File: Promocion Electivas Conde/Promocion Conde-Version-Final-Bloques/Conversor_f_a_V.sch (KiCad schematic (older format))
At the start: 14 parts, among them J2 Bornera Señal de Entrada, Q1 BC848, U2 4040, U3 4070, U4 TL082

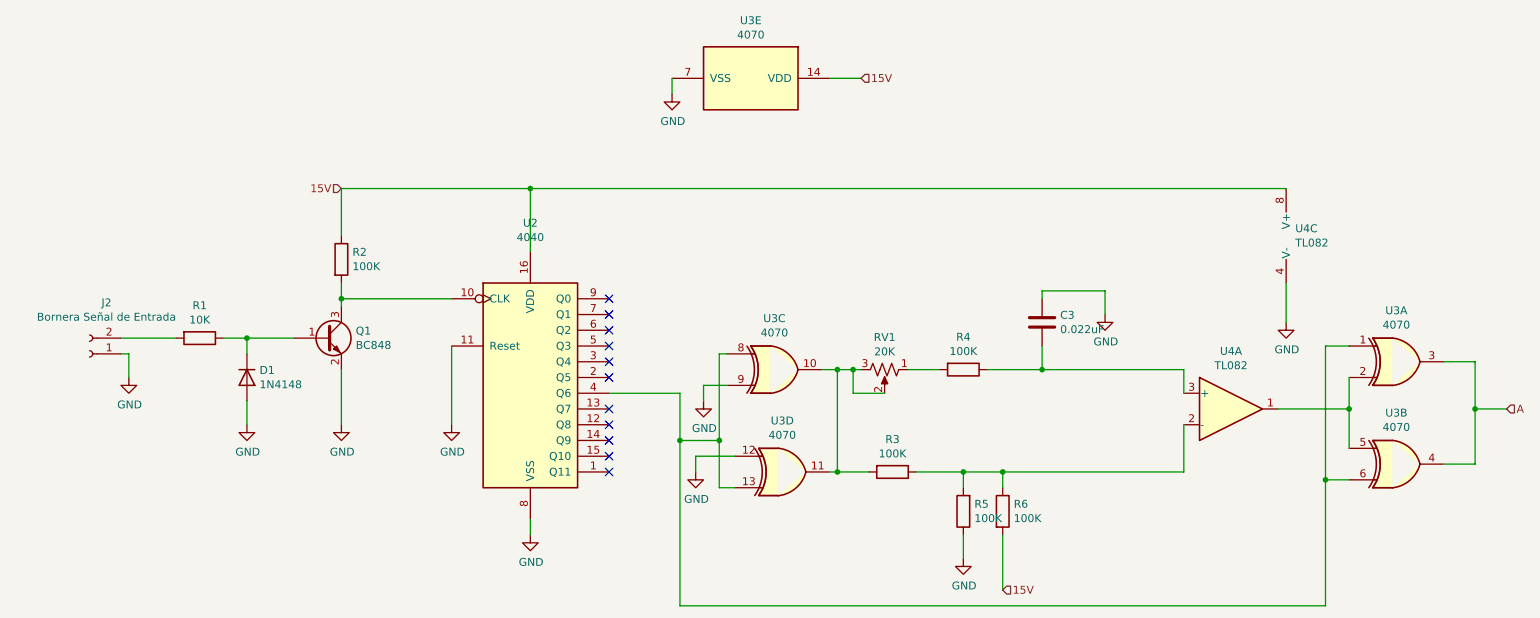
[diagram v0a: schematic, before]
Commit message: Agregue circuito 4-20 mA a la version en bloques
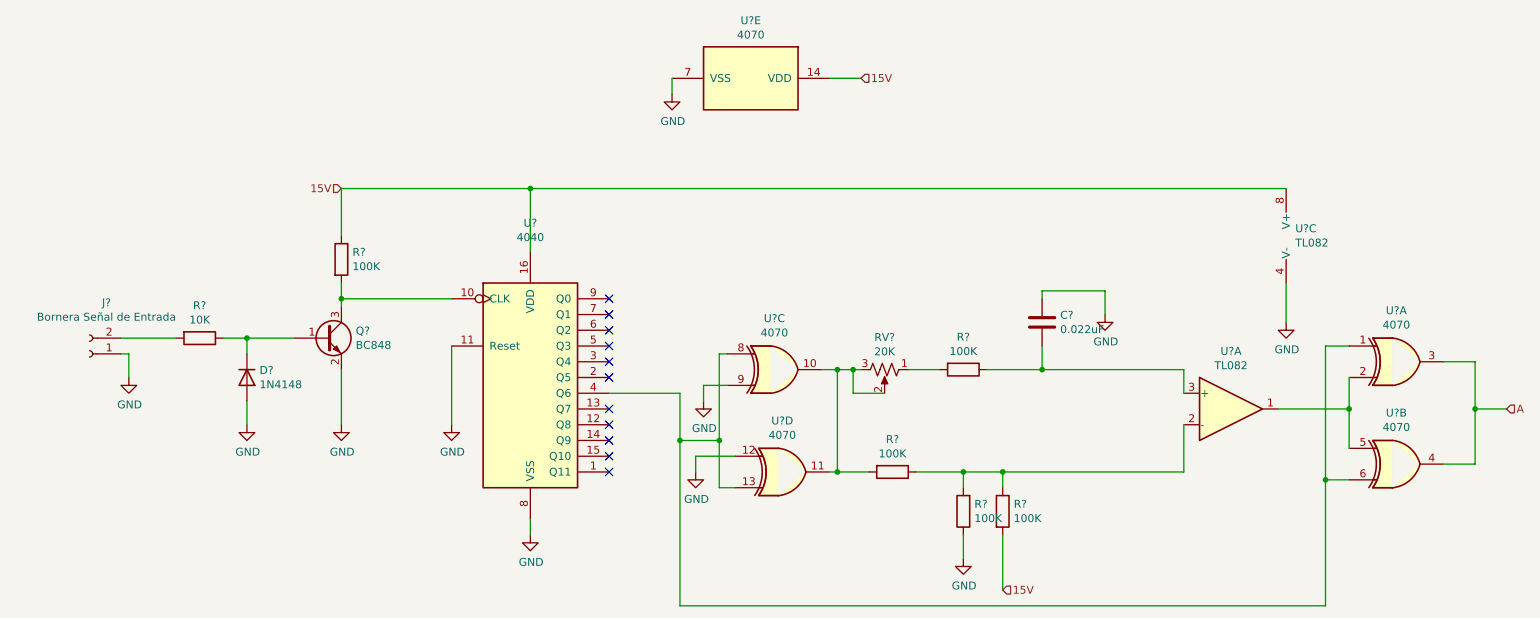
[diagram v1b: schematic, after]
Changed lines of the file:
@@
 $Descr A4 11693 8268
 encoding utf-8
-Sheet 2 4
+Sheet 5 5
 Title ""
 Date ""
@@
 AR Path="/61312797" Ref="R?"  Part="1"
 AR Path="/612E15A4/61312797" Ref="R2"  Part="1"
-F 0 "R2" H 2920 2146 50  0000 L CNN
+AR Path="/6184FF73/61312797" Ref="R?"  Part="1"
+F 0 "R?" H 2920 2146 50  0000 L CNN
 F 1 "100K" H 2920 2055 50  0000 L CNN
 F 2 "Resistor_SMD:R_0603_1608Metric_Pad0.98x0.95mm_HandSolder" V 2780 2100 50  0001 C CNN
@@
 AR Path="/6131279D" Ref="Q?"  Part="1"
 AR Path="/612E15A4/6131279D" Ref="Q1"  Part="1"
-F 0 "Q1" H 2941 2646 50  0000 L CNN
+AR Path="/6184FF73/6131279D" Ref="Q?"  Part="1"
+F 0 "Q?" H 2941 2646 50  0000 L CNN
 F 1 "BC848" H 2941 2555 50  0000 L CNN
 F 2 "Package_TO_SOT_SMD:SOT-23" H 2950 2525 50  0001 L CIN
@@
 AR Path="/613127A3" Ref="D?"  Part="1"
 AR Path="/612E15A4/613127A3" Ref="D1"  Part="1"
-F 0 "D1" V 2204 2930 50  0000 L CNN
+AR Path="/6184FF73/613127A3" Ref="D?"  Part="1"
+F 0 "D?" V 2204 2930 50  0000 L CNN
 F 1 "1N4148" V 2295 2930 50  0000 L CNN
 F 2 "Diode_THT:D_DO-35_SOD27_P7.62mm_Horizontal" H 2250 2675 50  0001 C CNN
@@
 AR Path="/613127A9" Ref="R?"  Part="1"
 AR Path="/612E15A4/613127A9" Ref="R1"  Part="1"
-F 0 "R1" V 1743 2600 50  0000 C CNN
+AR Path="/6184FF73/613127A9" Ref="R?"  Part="1"
+F 0 "R?" V 1743 2600 50  0000 C CNN
 F 1 "10K" V 1834 2600 50  0000 C CNN
 F 2 "Resistor_SMD:R_0603_1608Metric_Pad0.98x0.95mm_HandSolder" V 1880 2600 50  0001 C CNN
@@
 AR Path="/613127AF" Ref="#PWR?"  Part="1"
 AR Path="/612E15A4/613127AF" Ref="#PWR0101"  Part="1"
-F 0 "#PWR0101" H 2250 2900 50  0001 C CNN
+AR Path="/6184FF73/613127AF" Ref="#PWR?"  Part="1"
+F 0 "#PWR?" H 2250 2900 50  0001 C CNN
 F 1 "GND" H 2255 2977 50  0000 C CNN
 F 2 "" H 2250 3150 50  0001 C CNN
@@
 AR Path="/613127B5" Ref="#PWR?"  Part="1"
 AR Path="/612E15A4/613127B5" Ref="#PWR0102"  Part="1"
-F 0 "#PWR0102" H 2850 2900 50  0001 C CNN
+AR Path="/6184FF73/613127B5" Ref="#PWR?"  Part="1"
+F 0 "#PWR?" H 2850 2900 50  0001 C CNN
 F 1 "GND" H 2855 2977 50  0000 C CNN
 F 2 "" H 2850 3150 50  0001 C CNN
@@
 AR Path="/613127BB" Ref="U?"  Part="1"
 AR Path="/612E15A4/613127BB" Ref="U2"  Part="1"
-F 0 "U2" H 4050 3831 50  0000 C CNN
+AR Path="/6184FF73/613127BB" Ref="U?"  Part="1"
+F 0 "U?" H 4050 3831 50  0000 C CNN
 F 1 "4040" H 4050 3740 50  0000 C CNN
 F 2 "Package_SO:SOIC-16_3.9x9.9mm_P1.27mm" H 4050 2850 50  0001 C CNN
@@
 AR Path="/613127C1" Ref="#PWR?"  Part="1"
 AR Path="/612E15A4/613127C1" Ref="#PWR0103"  Part="1"
-F 0 "#PWR0103" H 3550 2900 50  0001 C CNN
+AR Path="/6184FF73/613127C1" Ref="#PWR?"  Part="1"
+F 0 "#PWR?" H 3550 2900 50  0001 C CNN
 F 1 "GND" H 3555 2977 50  0000 C CNN
 F 2 "" H 3550 3150 50  0001 C CNN
@@
 AR Path="/613127C7" Ref="#PWR?"  Part="1"
 AR Path="/612E15A4/613127C7" Ref="#PWR0104"  Part="1"
-F 0 "#PWR0104" H 4050 3600 50  0001 C CNN
+AR Path="/6184FF73/613127C7" Ref="#PWR?"  Part="1"
+F 0 "#PWR?" H 4050 3600 50  0001 C CNN
 F 1 "GND" H 4055 3677 50  0000 C CNN
 F 2 "" H 4050 3850 50  0001 C CNN
@@
 AR Path="/613127CD" Ref="U?"  Part="1"
 AR Path="/612E15A4/613127CD" Ref="U3"  Part="1"
-F 0 "U3" H 9550 3075 50  0000 C CNN
+AR Path="/6184FF73/613127CD" Ref="U?"  Part="1"
+F 0 "U?" H 9550 3075 50  0000 C CNN
 F 1 "4070" H 9550 2984 50  0000 C CNN
 F 2 "" H 9550 2750 50  0001 C CNN
@@
 AR Path="/613127D3" Ref="U?"  Part="2"
 AR Path="/612E15A4/613127D3" Ref="U3"  Part="2"
-F 0 "U3" H 9550 3725 50  0000 C CNN
+AR Path="/6184FF73/613127D3" Ref="U?"  Part="2"
+F 0 "U?" H 9550 3725 50  0000 C CNN
 F 1 "4070" H 9550 3634 50  0000 C CNN
 F 2 "" H 9550 3400 50  0001 C CNN
@@
 AR Path="/613127D9" Ref="U?"  Part="3"
 AR Path="/612E15A4/613127D9" Ref="U3"  Part="3"
-F 0 "U3" H 5600 3125 50  0000 C CNN
+AR Path="/6184FF73/613127D9" Ref="U?"  Part="3"
+F 0 "U?" H 5600 3125 50  0000 C CNN
 F 1 "4070" H 5600 3034 50  0000 C CNN
 F 2 "" H 5600 2800 50  0001 C CNN
@@
 AR Path="/613127DF" Ref="U?"  Part="5"
 AR Path="/612E15A4/613127DF" Ref="U3"  Part="5"
-F 0 "U3" V 5083 950 50  0000 C CNN
+AR Path="/6184FF73/613127DF" Ref="U?"  Part="5"
+F 0 "U?" V 5083 950 50  0000 C CNN
 F 1 "4070" V 5174 950 50  0000 C CNN
 F 2 "" H 5450 950 50  0001 C CNN
@@
 AR Path="/613127E5" Ref="R?"  Part="1"
 AR Path="/612E15A4/613127E5" Ref="R3"  Part="1"
-F 0 "R3" V 6143 3450 50  0000 C CNN
+AR Path="/6184FF73/613127E5" Ref="R?"  Part="1"
+F 0 "R?" V 6143 3450 50  0000 C CNN
 F 1 "100K" V 6234 3450 50  0000 C CNN
 F 2 "Resistor_SMD:R_0603_1608Metric_Pad0.98x0.95mm_HandSolder" V 6280 3450 50  0001 C CNN
@@
 AR Path="/613127EB" Ref="R?"  Part="1"
 AR Path="/612E15A4/613127EB" Ref="R5"  Part="1"
-F 0 "R5" H 6730 3654 50  0000 R CNN
+AR Path="/6184FF73/613127EB" Ref="R?"  Part="1"
+F 0 "R?" H 6730 3654 50  0000 R CNN
 F 1 "100K" H 6730 3745 50  0000 R CNN
 F 2 "Resistor_SMD:R_0603_1608Metric_Pad0.98x0.95mm_HandSolder" V 6730 3700 50  0001 C CNN
@@
 AR Path="/613127F1" Ref="R?"  Part="1"
 AR Path="/612E15A4/613127F1" Ref="R6"  Part="1"
-F 0 "R6" H 7120 3746 50  0000 L CNN
+AR Path="/6184FF73/613127F1" Ref="R?"  Part="1"
+F 0 "R?" H 7120 3746 50  0000 L CNN
 F 1 "100K" H 7120 3655 50  0000 L CNN
 F 2 "Resistor_SMD:R_0603_1608Metric_Pad0.98x0.95mm_HandSolder" V 6980 3700 50  0001 C CNN
@@
 AR Path="/613127F7" Ref="R?"  Part="1"
 AR Path="/612E15A4/613127F7" Ref="R4"  Part="1"
-F 0 "R4" V 6593 2800 50  0000 C CNN
+AR Path="/6184FF73/613127F7" Ref="R?"  Part="1"
+F 0 "R?" V 6593 2800 50  0000 C CNN
 F 1 "100K" V 6684 2800 50  0000 C CNN
 F 2 "Resistor_SMD:R_0603_1608Metric_Pad0.98x0.95mm_HandSolder" V 6730 2800 50  0001 C CNN
@@
 AR Path="/613127FD" Ref="U?"  Part="1"
 AR Path="/612E15A4/613127FD" Ref="U4"  Part="1"
-F 0 "U4" H 8500 3417 50  0000 C CNN
+AR Path="/6184FF73/613127FD" Ref="U?"  Part="1"
+F 0 "U?" H 8500 3417 50  0000 C CNN
 F 1 "TL082" H 8500 3326 50  0000 C CNN
 F 2 "Package_SO:SOIC-8-1EP_3.9x4.9mm_P1.27mm_EP2.29x3mm" H 8500 3050 50  0001 C CNN
@@
 AR Path="/61312803" Ref="J?"  Part="1"
 AR Path="/612E15A4/61312803" Ref="J2"  Part="1"
-F 0 "J2" H 1142 2375 50  0000 C CNN
+AR Path="/6184FF73/61312803" Ref="J?"  Part="1"
+F 0 "J?" H 1142 2375 50  0000 C CNN
 F 1 "Bornera Señal de Entrada" H 1142 2466 50  0000 C CNN
 F 2 "" H 1250 2700 50  0001 C CNN
@@
 AR Path="/61312815" Ref="#PWR?"  Part="1"
 AR Path="/612E15A4/61312815" Ref="#PWR0105"  Part="1"
-F 0 "#PWR0105" H 5100 3200 50  0001 C CNN
+AR Path="/6184FF73/61312815" Ref="#PWR?"  Part="1"
+F 0 "#PWR?" H 5100 3200 50  0001 C CNN
 F 1 "GND" H 5105 3277 50  0000 C CNN
 F 2 "" H 5100 3450 50  0001 C CNN
@@
 AR Path="/6131281B" Ref="#PWR?"  Part="1"
 AR Path="/612E15A4/6131281B" Ref="#PWR0106"  Part="1"
-F 0 "#PWR0106" H 5150 2750 50  0001 C CNN
+AR Path="/6184FF73/6131281B" Ref="#PWR?"  Part="1"
+F 0 "#PWR?" H 5150 2750 50  0001 C CNN
 F 1 "GND" H 5155 2827 50  0000 C CNN
 F 2 "" H 5150 3000 50  0001 C CNN
@@
 AR Path="/61312824" Ref="RV?"  Part="1"
 AR Path="/612E15A4/61312824" Ref="RV1"  Part="1"
-F 0 "RV1" V 6095 2800 50  0000 C CNN
+AR Path="/6184FF73/61312824" Ref="RV?"  Part="1"
+F 0 "RV?" V 6095 2800 50  0000 C CNN
 F 1 "20K" V 6186 2800 50  0000 C CNN
 F 2 "" H 6300 2800 50  0001 C CNN
@@
 AR Path="/6131282E" Ref="C?"  Part="1"
 AR Path="/612E15A4/6131282E" Ref="C3"  Part="1"
-F 0 "C3" H 7415 2546 50  0000 L CNN
+AR Path="/6184FF73/6131282E" Ref="C?"  Part="1"
+F 0 "C?" H 7415 2546 50  0000 L CNN
 F 1 "0.022uF" H 7415 2455 50  0000 L CNN
 F 2 "Capacitor_SMD:C_0603_1608Metric_Pad1.08x0.95mm_HandSolder" H 7338 2350 50  0001 C CNN
@@
 AR Path="/61312836" Ref="U?"  Part="4"
 AR Path="/612E15A4/61312836" Ref="U3"  Part="4"
-F 0 "U3" H 5650 3775 50  0000 C CNN
+AR Path="/6184FF73/61312836" Ref="U?"  Part="4"
+F 0 "U?" H 5650 3775 50  0000 C CNN
 F 1 "4070" H 5650 3684 50  0000 C CNN
 F 2 "" H 5650 3450 50  0001 C CNN
@@
 AR Path="/61312847" Ref="#PWR?"  Part="1"
 AR Path="/612E15A4/61312847" Ref="#PWR0107"  Part="1"
-F 0 "#PWR0107" H 6800 3750 50  0001 C CNN
+AR Path="/6184FF73/61312847" Ref="#PWR?"  Part="1"
+F 0 "#PWR?" H 6800 3750 50  0001 C CNN
 F 1 "GND" H 6805 3827 50  0000 C CNN
 F 2 "" H 6800 4000 50  0001 C CNN
@@
 AR Path="/61312853" Ref="#PWR?"  Part="1"
 AR Path="/612E15A4/61312853" Ref="#PWR0108"  Part="1"
-F 0 "#PWR0108" H 7700 2200 50  0001 C CNN
+AR Path="/6184FF73/61312853" Ref="#PWR?"  Part="1"
+F 0 "#PWR?" H 7700 2200 50  0001 C CNN
 F 1 "GND" H 7705 2277 50  0000 C CNN
 F 2 "" H 7700 2450 50  0001 C CNN
@@
 AR Path="/6131285F" Ref="U?"  Part="3"
 AR Path="/612E15A4/6131285F" Ref="U4"  Part="3"
-F 0 "U4" H 8908 1996 50  0000 L CNN
+AR Path="/6184FF73/6131285F" Ref="U?"  Part="3"
+F 0 "U?" H 8908 1996 50  0000 L CNN
 F 1 "TL082" H 8908 1905 50  0000 L CNN
 F 2 "Package_SO:SOIC-8-1EP_3.9x4.9mm_P1.27mm_EP2.29x3mm" H 8950 1950 50  0001 C CNN
@@
 AR Path="/61312865" Ref="#PWR?"  Part="1"
 AR Path="/612E15A4/61312865" Ref="#PWR0109"  Part="1"
-F 0 "#PWR0109" H 8850 2250 50  0001 C CNN
+AR Path="/6184FF73/61312865" Ref="#PWR?"  Part="1"
+F 0 "#PWR?" H 8850 2250 50  0001 C CNN
 F 1 "GND" H 8855 2327 50  0000 C CNN
 F 2 "" H 8850 2500 50  0001 C CNN
@@
 AR Path="/6131287A" Ref="#PWR?"  Part="1"
 AR Path="/612E15A4/6131287A" Ref="#PWR0110"  Part="1"
-F 0 "#PWR0110" H 4950 800 50  0001 C CNN
+AR Path="/6184FF73/6131287A" Ref="#PWR?"  Part="1"
+F 0 "#PWR?" H 4950 800 50  0001 C CNN
 F 1 "GND" H 4955 877 50  0000 C CNN
 F 2 "" H 4950 1050 50  0001 C CNN
@@
 AR Path="/613128BC" Ref="#PWR?"  Part="1"
 AR Path="/612E15A4/613128BC" Ref="#PWR0111"  Part="1"
-F 0 "#PWR0111" H 1500 2600 50  0001 C CNN
+AR Path="/6184FF73/613128BC" Ref="#PWR?"  Part="1"
+F 0 "#PWR?" H 1500 2600 50  0001 C CNN
 F 1 "GND" H 1505 2677 50  0000 C CNN
 F 2 "" H 1500 2850 50  0001 C CNN
